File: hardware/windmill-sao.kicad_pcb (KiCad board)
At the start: 2 copper layers, 49.2 x 48.2 mm, 32 parts, among them J1 SAO, J2 QWIIC, M1 SG90, U1 CH32V003F4P6

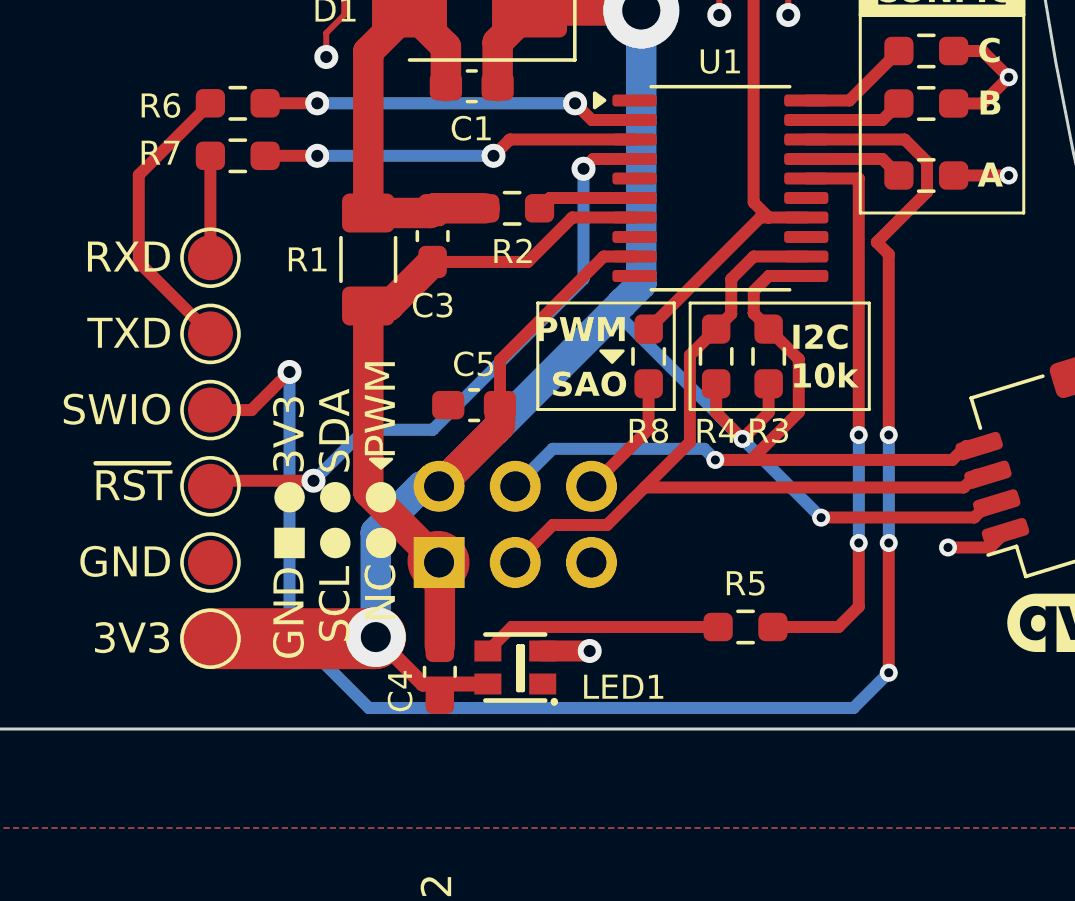
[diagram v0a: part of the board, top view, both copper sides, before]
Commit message: Fix thermal release violations
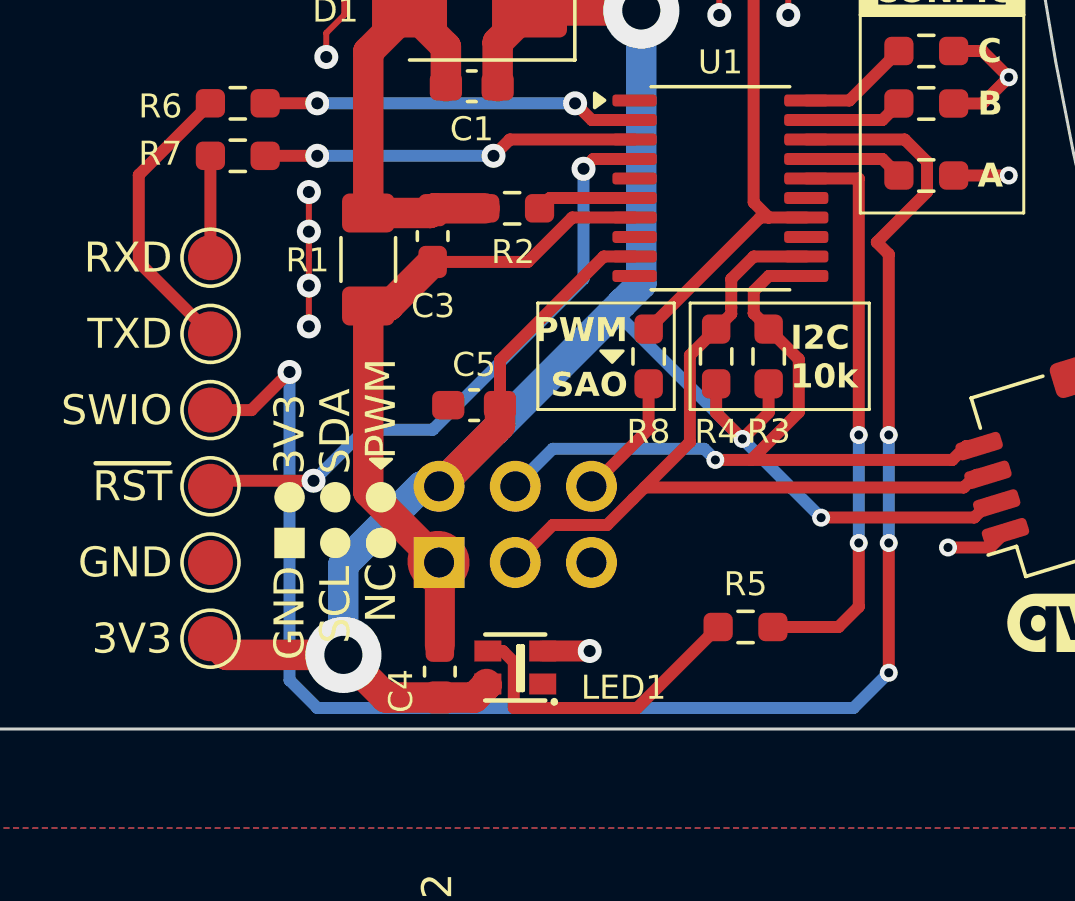
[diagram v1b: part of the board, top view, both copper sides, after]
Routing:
- net GND: track 51.0 -> 55.4 mm, vias 21 -> 25
- net Net-(LED1-DI): track 8.01 -> 10.5 mm
- net +3V3: track 80.0 -> 81.4 mm
- net SWIO: track 55.5 -> 56.5 mm

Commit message: Add OSHWA cert no. to silkscreen
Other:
- board text added: "PL000026"
